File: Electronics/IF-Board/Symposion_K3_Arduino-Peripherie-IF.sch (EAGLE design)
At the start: 22 parts, among them J1 22-27-2051-05, J2 22-27-2051-05, J3 22-27-2051-05, J4 22-27-2051-05, J5 22-27-2051-05, J6 22-27-2051-05, Q1 0_WSH_FAVORITES_BUZ11BV, Q2 0_WSH_FAVORITES_BUZ11BV, Q3 0_WSH_FAVORITES_BUZ11BV, Q4 0_WSH_FAVORITES_BUZ11BV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

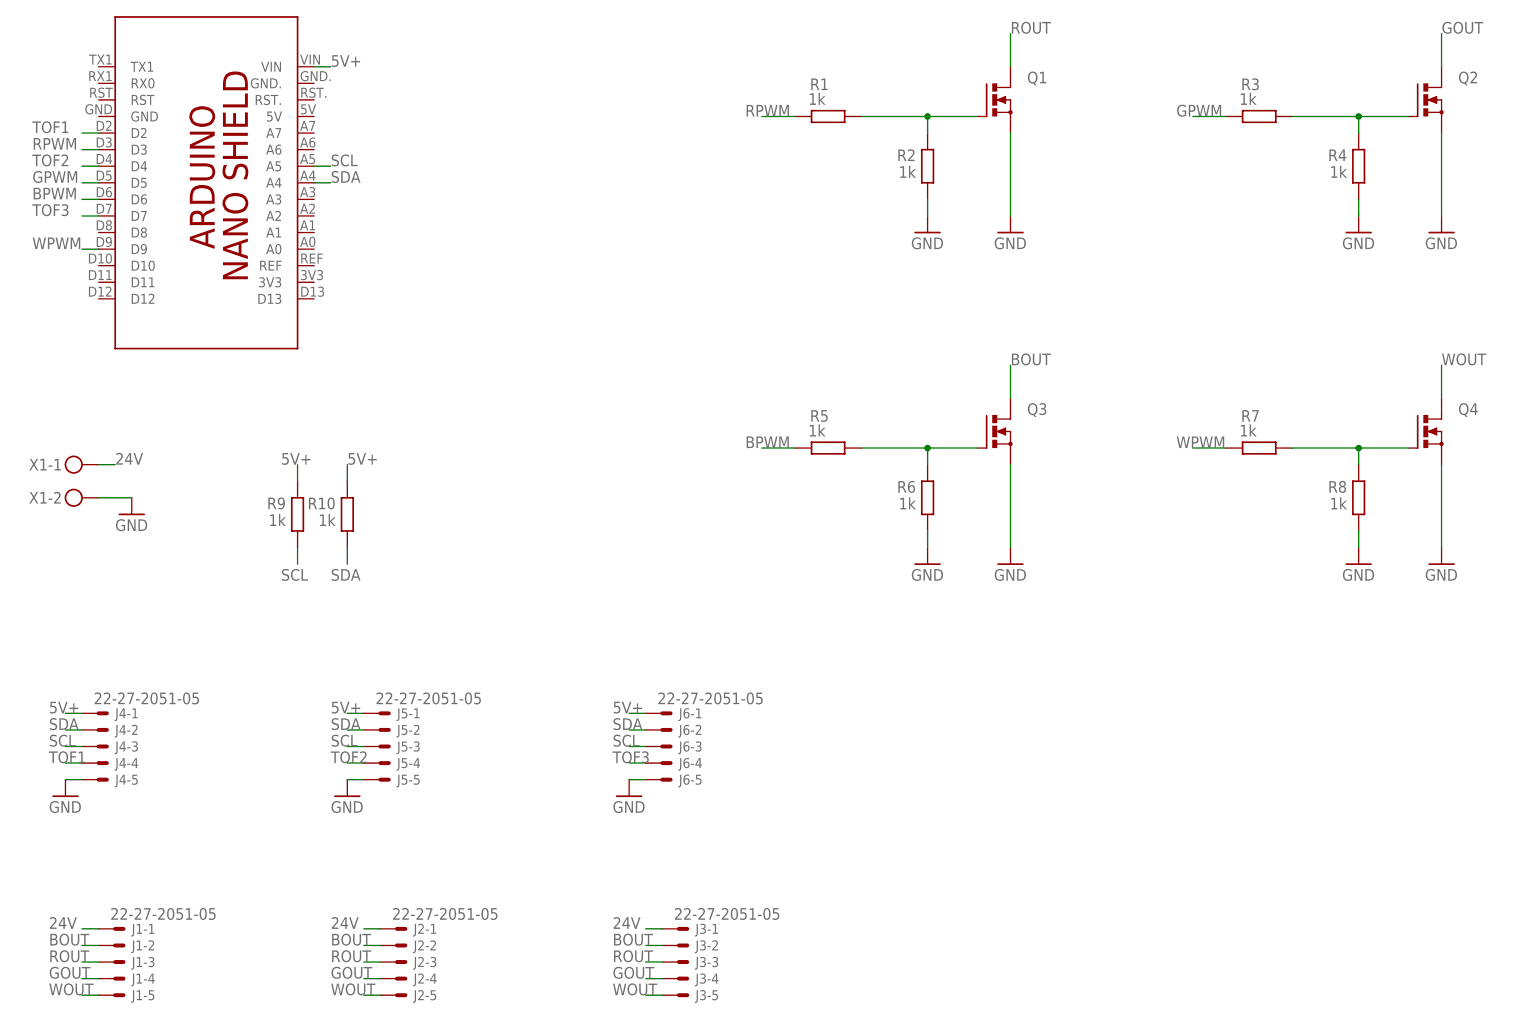
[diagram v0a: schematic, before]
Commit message: Schematic v1.6
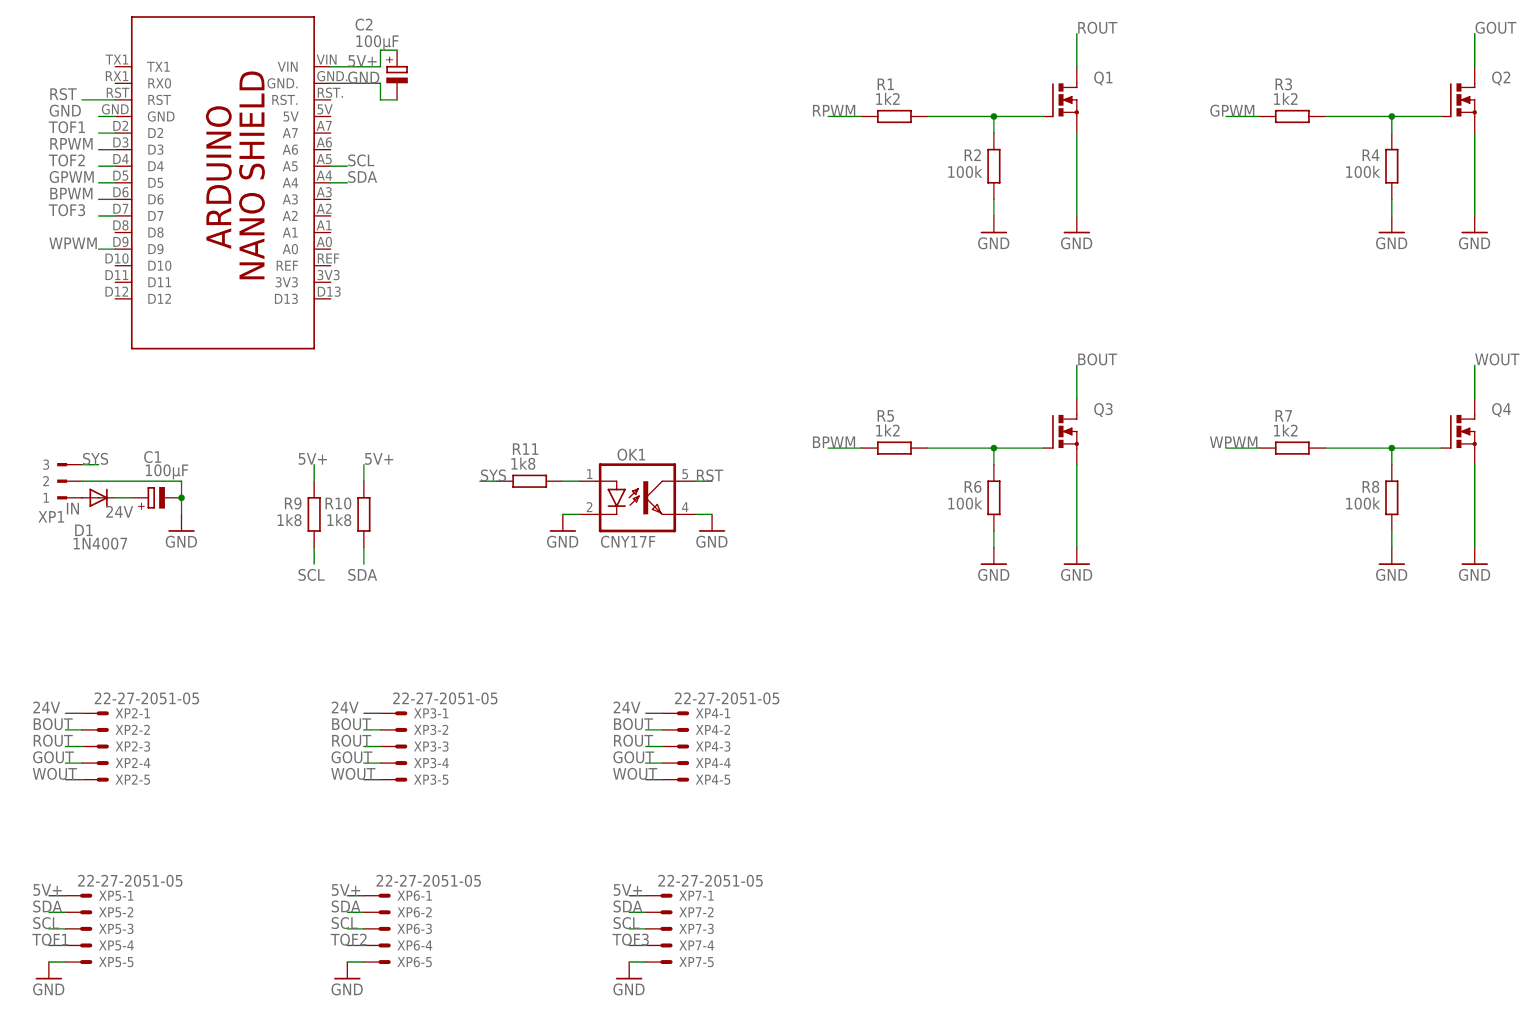
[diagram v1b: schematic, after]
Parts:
- removed J1, J2, J3, J5, J6: 22-27-2051-05, con-molex:22-27-2051-05
- removed X1: 0_WSH_FAVORITES_MKDSN1,5/2-5,08, 20221130_WSH_Eagle_Lib:0_WSH_FAVORITES_MKDSN1,5/2-5,08
- added C1, C2: 100µF, 20221130_WSH_Eagle_Lib:RCL_CPOL-EUE5-6
- added D1: 1N4007, 20221130_WSH_Eagle_Lib:DIODE_DIODE-F126-10
- added OK1: CNY17F, optocoupler:CNY17F
- added R11: 1k8, resistor:R-EU_R1206
- added XP1: 180-3, con-weidmueller-sl35:180-3
- added XP3, XP4, XP5, XP6, XP7: 22-27-2051-05, con-molex:22-27-2051-05
- R1, R3, R5, R7: value 1k -> 1k2
- R10, R9: value 1k -> 1k8
- R2, R4, R6, R8: value 1k -> 100k
- renumbered J4 to XP2
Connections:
- new net IN: D1.A, XP1.1
- new net N$2: OK1.A, R11.1
- new net RST: OK1.COL, PCB1.RST
- new net SYS: R11.2, XP1.3
- net 24V: now also C1.+, D1.C, XP2-1.S, XP3-1.S, XP4-1.S; no longer J1-1.S, J2-1.S, J3-1.S, X1-1.KL
- net 5V+: now also C2.+, XP5-1.S, XP6-1.S, XP7-1.S; no longer J5-1.S, J6-1.S, XP2-1.S
- net BOUT: now also XP2-2.S, XP3-2.S, XP4-2.S; no longer J1-2.S, J2-2.S, J3-2.S
- net GND: now also C1.-, C2.-, OK1.C, OK1.EMIT, PCB1.GND, PCB1.GND., XP1.2, XP5-5.S, XP6-5.S, XP7-5.S; no longer J5-5.S, J6-5.S, X1-2.KL, XP2-5.S
- net GOUT: now also XP2-4.S, XP3-4.S, XP4-4.S; no longer J1-4.S, J2-4.S, J3-4.S
- net ROUT: now also XP2-3.S, XP3-3.S, XP4-3.S; no longer J1-3.S, J2-3.S, J3-3.S
- net SCL: now also XP5-3.S, XP6-3.S, XP7-3.S; no longer J5-3.S, J6-3.S, XP2-3.S
- net SDA: now also XP5-2.S, XP6-2.S, XP7-2.S; no longer J5-2.S, J6-2.S, XP2-2.S
- net TOF1: now also XP5-4.S; no longer XP2-4.S
- net TOF2: now also XP6-4.S; no longer J5-4.S
- net TOF3: now also XP7-4.S; no longer J6-4.S
- net WOUT: now also XP2-5.S, XP3-5.S, XP4-5.S; no longer J1-5.S, J2-5.S, J3-5.S
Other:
- moved on the sheet: Q1, Q2, Q3, Q4, R1, R10, R2, R3, R4, R5, R6, R7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
